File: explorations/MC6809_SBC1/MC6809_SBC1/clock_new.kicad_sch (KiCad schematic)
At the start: 28 parts, among them U2 74LS04, U3 MC6809, Y2 3.6864 MHz, Y3 3.6864 MHz

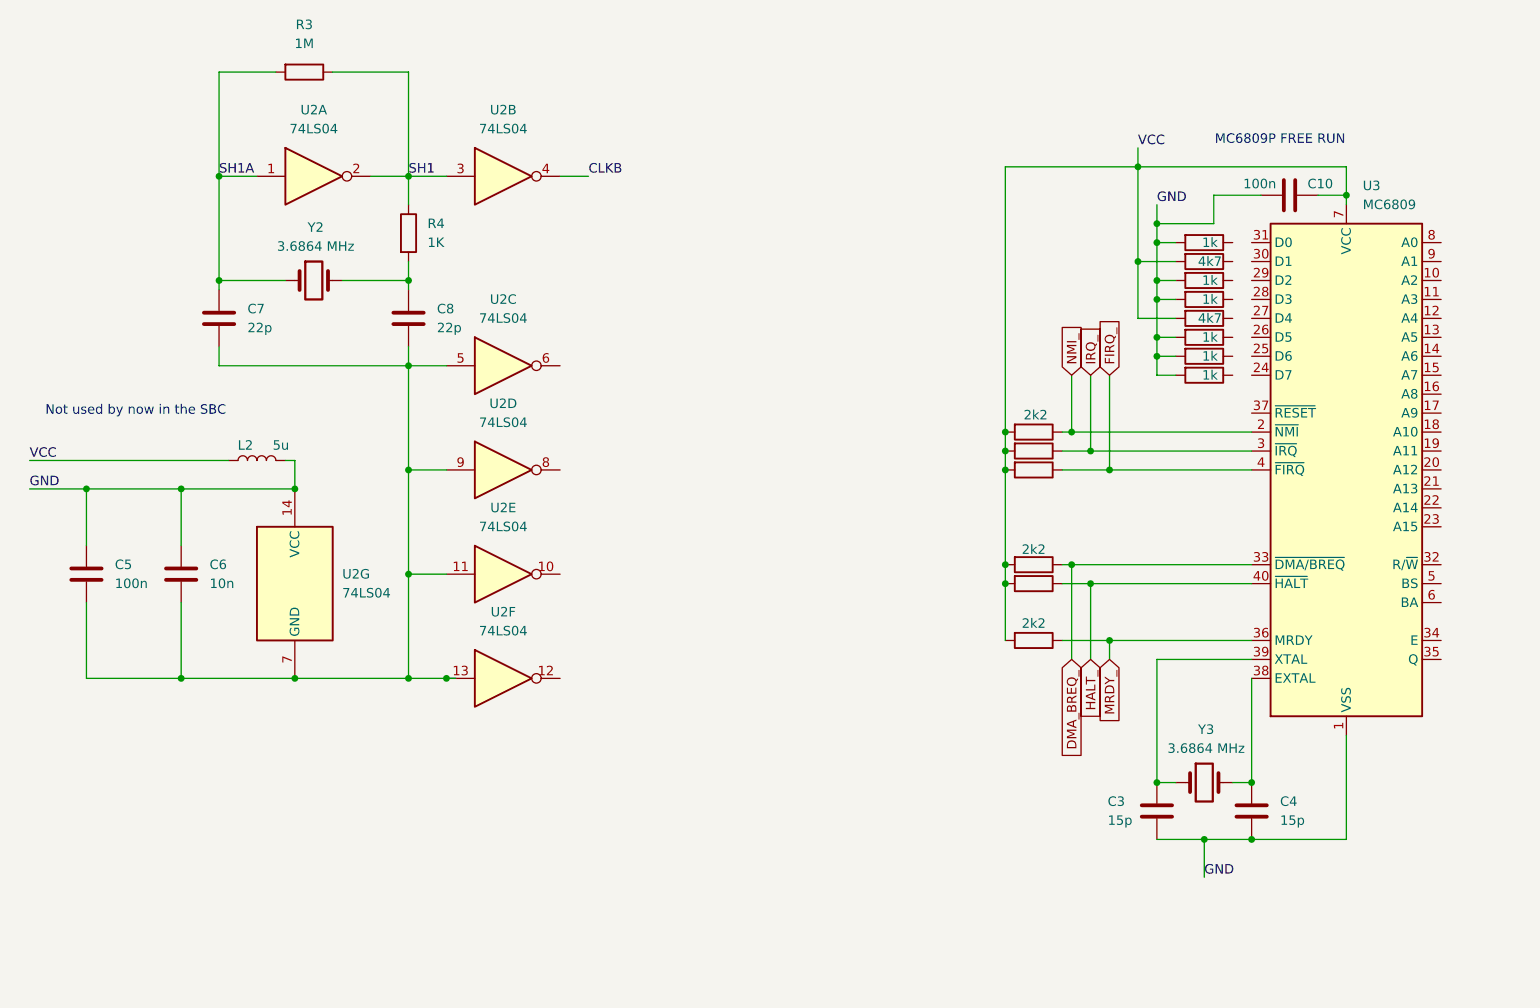
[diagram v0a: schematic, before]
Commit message: SBC1 scheme a& other stuff
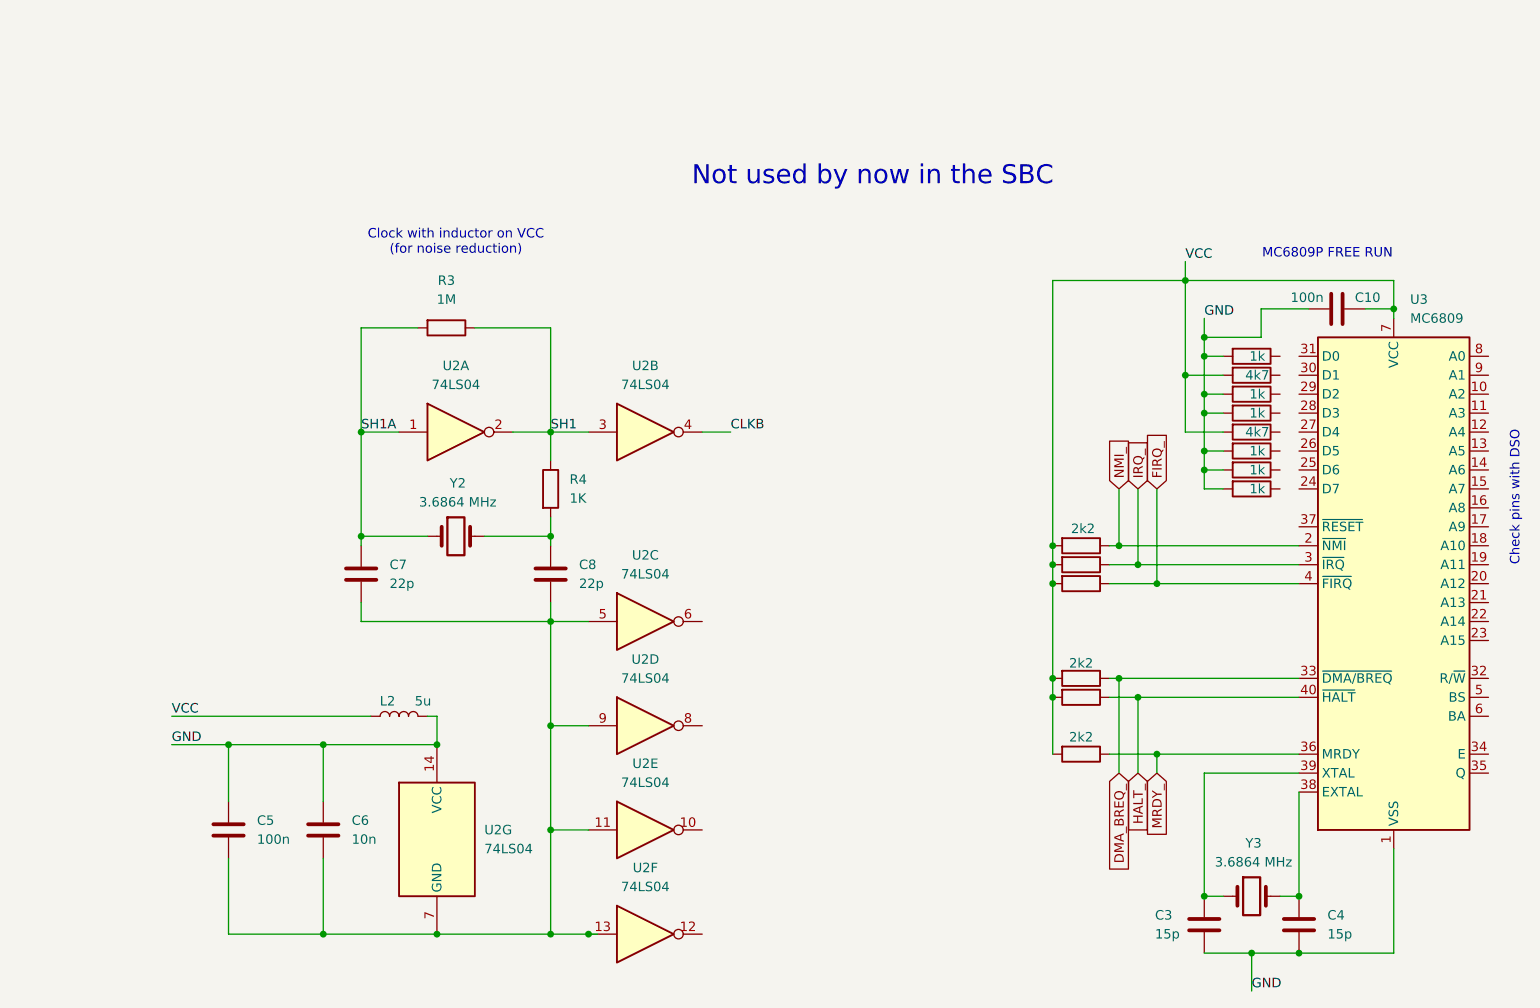
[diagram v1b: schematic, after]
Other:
- note added: "Check pins with DSO"
- note added: "Clock with inductor on VCC (for noise reduction)"
- moved on the sheet: C10, C3, C4, C5, C6, C7, C8, L2, R3, R4, U2A, U2B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
